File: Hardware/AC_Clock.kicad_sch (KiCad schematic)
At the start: 30 parts, among them J1 L, J2 N, J5 Minutes, J6 Hours, J7 PWR, J8 PWR, SW3 Hour Set, SW4 Min Set, T1 F12-500-C2, U1 AZ1117-5.0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

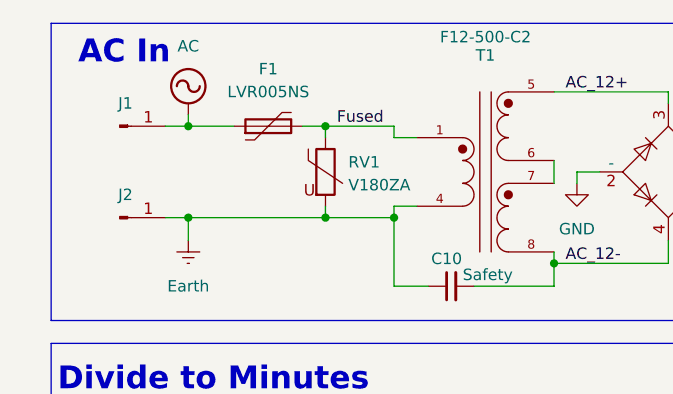
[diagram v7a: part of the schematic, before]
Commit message: Change to fuse of correct value
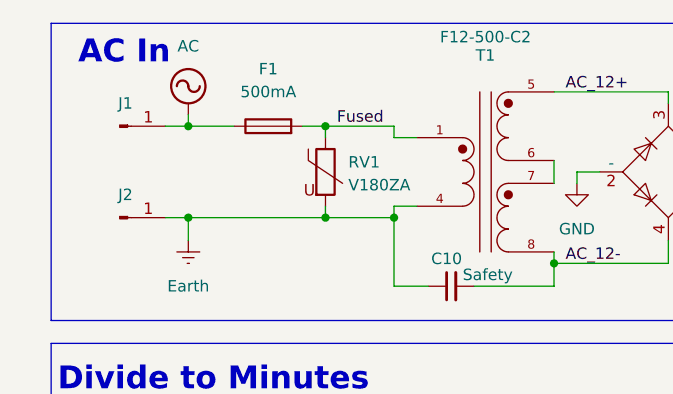
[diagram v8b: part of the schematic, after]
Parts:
- F1: value LVR005NS -> 500mA; footprint Fuse:Fuse_BelFuse_0ZRE0005FF_L8.3mm_W3.8mm -> JKC_Library:Fuse_Schurter_MST_250; symbol Device:Polyfuse -> Device:Fuse; MPN (none) -> 0034.6612
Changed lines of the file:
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@@
 	)
 	(symbol
-		(lib_id "Device:Polyfuse")
+		(lib_id "Device:Fuse")
 		(at 39.37 26.67 90)
 		(unit 1)
@@
 			)
 		)
-		(property "Value" "LVR005NS"
+		(property "Value" "500mA"
 			(at 39.37 22.86 90)
 			(effects
@@
 			)
 		)
-		(property "Footprint" "Fuse:Fuse_BelFuse_0ZRE0005FF_L8.3mm_W3.8mm"
-			(at 44.45 25.4 0)
+		(property "Footprint" "JKC_Library:Fuse_Schurter_MST_250"
+			(at 39.37 28.448 90)
 			(effects
 				(font
 					(size 1.27 1.27)
 				)
-				(justify left)
 				(hide yes)
 			)
@@
 			)
 		)
-		(property "Description" "Resettable fuse, polymeric positive temperature coefficient"
+		(property "Description" "Fuse"
 			(at 39.37 26.67 0)
 			(effects
 				(font
+					(size 1.27 1.27)
+				)
+				(hide yes)
+			)
+		)
+		(property "MPN" "0034.6612"
+			(at 39.37 26.67 90)
+			(effects
+				(font
